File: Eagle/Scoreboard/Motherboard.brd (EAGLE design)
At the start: 67.3 x 92.7 mm, 27 parts

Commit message: Added capacitors for filtering
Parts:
- added C3, C4: 100n, capacitor-wima:C5B2.5
- C2: value 10u -> 47u
- moved REG 5.24 mm to (39.4, 73.7)
- moved C1 2.54 mm to (15.2, 77.5)
- moved C2 2.54 mm to (15.2, 68.6)
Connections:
- net 12V: now also C3.1
- net GND: now also C3.2, C4.2
- net VIN_9V: now also C4.1
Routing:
- net VIN_9V: track 40.2 -> 47.4 mm
- net 12V: track 36.9 -> 41.9 mm
- net GND: track 239.6 -> 244.4 mm
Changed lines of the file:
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@@
 <attribute name="OC_NEWARK" value="70K9898" x="60.96" y="40.64" size="1.778" layer="27" rot="R90" display="off"/>
 </element>
-<element name="C1" library="rcl" library_urn="urn:adsk.eagle:library:334" package="E2-4" package3d_urn="urn:adsk.eagle:package:23347/1" value="10u" x="17.78" y="77.47" rot="R270">
-<attribute name="SPICEPREFIX" value="C" x="17.78" y="77.47" size="1.778" layer="27" rot="R270" display="off"/>
-</element>
-<element name="C2" library="rcl" library_urn="urn:adsk.eagle:library:334" package="E2-4" package3d_urn="urn:adsk.eagle:package:23347/1" value="10u" x="17.78" y="68.58" rot="R90">
-<attribute name="SPICEPREFIX" value="C" x="17.78" y="68.58" size="1.778" layer="27" rot="R90" display="off"/>
+<element name="C1" library="rcl" library_urn="urn:adsk.eagle:library:334" package="E2-4" package3d_urn="urn:adsk.eagle:package:23347/1" value="10u" x="15.24" y="77.47" rot="R270">
+<attribute name="SPICEPREFIX" value="C" x="15.24" y="77.47" size="1.778" layer="27" rot="R270" display="off"/>
+</element>
+<element name="C2" library="rcl" library_urn="urn:adsk.eagle:library:334" package="E2-4" package3d_urn="urn:adsk.eagle:package:23347/1" value="47u" x="15.24" y="68.58" rot="R90">
+<attribute name="SPICEPREFIX" value="C" x="15.24" y="68.58" size="1.778" layer="27" rot="R90" display="off"/>
 </element>
 <element name="R1" library="resistor" library_urn="urn:adsk.eagle:library:348" package="0204/7" package3d_urn="urn:adsk.eagle:package:25945/1" value="10k" x="53.34" y="30.48" rot="R90"/>
@@
 <element name="R4" library="resistor" library_urn="urn:adsk.eagle:library:348" package="0204/7" package3d_urn="urn:adsk.eagle:package:25945/1" value="10k" x="45.72" y="30.48" rot="R90"/>
 <element name="R5" library="resistor" library_urn="urn:adsk.eagle:library:348" package="0204/7" package3d_urn="urn:adsk.eagle:package:25945/1" value="10k" x="40.64" y="30.48" rot="R90"/>
-<element name="REG" library="linear" library_urn="urn:adsk.eagle:library:262" package="TO220H" package3d_urn="urn:adsk.eagle:package:16414/1" value="LM7809" x="34.29" y="74.93" rot="R270"/>
+<element name="REG" library="linear" library_urn="urn:adsk.eagle:library:262" package="TO220H" package3d_urn="urn:adsk.eagle:package:16414/1" value="LM7809" x="39.37" y="73.66" rot="R270"/>
 <element name="SCORE" library="con-wago-500" library_urn="urn:adsk.eagle:library:195" package="W237-103" package3d_urn="urn:adsk.eagle:package:10691/1" value="" x="5.08" y="12.7" rot="R270">
 <attribute name="MF" value="" x="5.08" y="12.7" size="1.778" layer="27" rot="R270" display="off"/>
@@
 <attribute name="OC_NEWARK" value="70K9898" x="60.96" y="81.28" size="1.778" layer="27" rot="R90" display="off"/>
 </element>
+<element name="C3" library="capacitor-wima" library_urn="urn:adsk.eagle:library:116" package="C5B2.5" package3d_urn="urn:adsk.eagle:package:5426/1" value="100n" x="24.13" y="76.2" rot="R270"/>
+<element name="C4" library="capacitor-wima" library_urn="urn:adsk.eagle:library:116" package="C5B2.5" package3d_urn="urn:adsk.eagle:package:5426/1" value="100n" x="24.13" y="67.31" rot="R90"/>
 </elements>
 <signals>
@@
 <contactref element="R6" pad="2"/>
 <contactref element="LED" pad="2"/>
-<wire x1="17.78" y1="69.596" x2="13.97" y2="69.596" width="0.254" layer="16"/>
-<wire x1="13.97" y1="69.596" x2="4.786" y2="69.596" width="0.254" layer="16"/>
-<wire x1="4.786" y1="69.596" x2="3.81" y2="68.62" width="0.254" layer="16"/>
 <wire x1="19.09" y1="87.63" x2="19.09" y2="90.21" width="0.254" layer="16"/>
 <wire x1="19.09" y1="90.21" x2="20.32" y2="91.44" width="0.254" layer="16"/>
 <wire x1="20.32" y1="91.44" x2="29.21" y2="91.44" width="0.254" layer="16"/>
 <wire x1="29.21" y1="91.44" x2="33.02" y2="87.63" width="0.254" layer="16"/>
-<wire x1="17.78" y1="76.454" x2="17.78" y2="69.596" width="0.254" layer="16"/>
-<wire x1="17.78" y1="76.454" x2="19.304" y2="74.93" width="0.254" layer="16"/>
-<wire x1="19.304" y1="74.93" x2="24.13" y2="74.93" width="0.254" layer="16"/>
-<wire x1="24.13" y1="74.93" x2="30.48" y2="74.93" width="0.254" layer="16"/>
-<wire x1="30.48" y1="74.93" x2="33.02" y2="77.47" width="0.254" layer="16"/>
-<wire x1="33.02" y1="77.47" x2="33.02" y2="87.63" width="0.254" layer="16"/>
+<wire x1="33.02" y1="73.66" x2="35.56" y2="76.2" width="0.254" layer="16"/>
+<wire x1="35.56" y1="76.2" x2="35.56" y2="87.63" width="0.254" layer="16"/>
 <wire x1="20.32" y1="38.1" x2="24.13" y2="38.1" width="0.254" layer="16"/>
-<wire x1="13.97" y1="53.34" x2="16.51" y2="50.8" width="0.254" layer="16"/>
-<wire x1="16.51" y1="50.8" x2="22.86" y2="50.8" width="0.254" layer="16"/>
+<wire x1="22.86" y1="50.8" x2="16.51" y2="50.8" width="0.254" layer="16"/>
 <wire x1="22.86" y1="50.8" x2="24.13" y2="49.53" width="0.254" layer="16"/>
 <wire x1="24.13" y1="49.53" x2="24.13" y2="43.18" width="0.254" layer="16"/>
 <wire x1="24.13" y1="43.18" x2="24.13" y2="38.1" width="0.254" layer="16"/>
-<wire x1="13.97" y1="69.596" x2="13.97" y2="53.34" width="0.254" layer="16"/>
 <contactref element="433MHZ_VC" pad="1"/>
 <contactref element="INFRA_VC" pad="2"/>
@@
 <wire x1="65.837" y1="86.36" x2="65.837" y2="82.347" width="0.254" layer="16"/>
 <wire x1="65.837" y1="82.347" x2="62.23" y2="78.74" width="0.254" layer="16"/>
-<wire x1="47.03" y1="87.63" x2="33.02" y2="87.63" width="0.254" layer="16"/>
+<wire x1="47.03" y1="87.63" x2="35.56" y2="87.63" width="0.254" layer="16"/>
 <wire x1="40.64" y1="34.29" x2="43.18" y2="34.29" width="0.254" layer="16"/>
 <wire x1="43.18" y1="34.29" x2="45.72" y2="34.29" width="0.254" layer="16"/>
@@
 <vertex x="-2.54" y="93.98"/>
 </polygon>
+<contactref element="C3" pad="2"/>
+<contactref element="C4" pad="2"/>
+<wire x1="16.51" y1="50.8" x2="16.51" y2="53.34" width="0.3048" layer="16"/>
+<wire x1="16.51" y1="53.34" x2="10.16" y2="59.69" width="0.3048" layer="16"/>
+<wire x1="10.16" y1="59.69" x2="10.16" y2="69.596" width="0.3048" layer="16"/>
+<wire x1="35.56" y1="87.63" x2="33.02" y2="87.63" width="0.254" layer="16"/>
+<wire x1="29.21" y1="73.66" x2="24.13" y2="73.66" width="1.016" layer="16"/>
+<wire x1="24.13" y1="73.66" x2="24.13" y2="69.85" width="1.016" layer="16"/>
+<wire x1="15.24" y1="76.454" x2="15.24" y2="69.596" width="1.016" layer="16"/>
+<wire x1="15.24" y1="69.596" x2="4.786" y2="69.596" width="1.016" layer="16"/>
+<wire x1="4.786" y1="69.596" x2="3.81" y2="68.62" width="1.016" layer="16"/>
+<wire x1="15.24" y1="69.596" x2="23.876" y2="69.596" width="1.016" layer="16"/>
+<wire x1="23.876" y1="69.596" x2="24.13" y2="69.85" width="1.016" layer="16"/>
 </signal>
 <signal name="N$1">
@@
 <contactref element="R7" pad="2"/>
 <wire x1="8.93" y1="87.63" x2="13.93" y2="87.63" width="1.016" layer="16"/>
-<wire x1="24.09" y1="87.63" x2="24.13" y2="87.59" width="1.016" layer="16"/>
-<wire x1="24.13" y1="87.59" x2="24.13" y2="78.74" width="1.016" layer="16"/>
-<wire x1="24.13" y1="78.74" x2="24.13" y2="77.47" width="1.016" layer="16"/>
-<wire x1="11.557" y1="78.613" x2="13.97" y2="78.613" width="1.016" layer="16"/>
-<wire x1="13.97" y1="78.613" x2="17.653" y2="78.613" width="1.016" layer="16"/>
-<wire x1="17.653" y1="78.613" x2="17.78" y2="78.486" width="1.016" layer="16"/>
-<wire x1="17.78" y1="78.486" x2="23.876" y2="78.486" width="1.016" layer="16"/>
-<wire x1="23.876" y1="78.486" x2="24.13" y2="78.74" width="1.016" layer="16"/>
+<wire x1="13.97" y1="78.613" x2="15.24" y2="78.613" width="1.016" layer="16"/>
+<wire x1="15.24" y1="78.613" x2="15.24" y2="78.486" width="1.016" layer="16"/>
 <wire x1="13.93" y1="87.63" x2="13.93" y2="78.653" width="1.016" layer="16"/>
 <wire x1="13.93" y1="78.653" x2="13.97" y2="78.613" width="1.016" layer="16"/>
+<contactref element="C3" pad="1"/>
+<wire x1="11.557" y1="78.613" x2="13.97" y2="78.613" width="1.016" layer="16"/>
+<wire x1="15.24" y1="78.486" x2="15.494" y2="78.74" width="1.016" layer="16"/>
+<wire x1="15.494" y1="78.74" x2="24.13" y2="78.74" width="1.016" layer="16"/>
+<wire x1="24.13" y1="78.74" x2="26.67" y2="78.74" width="1.016" layer="16"/>
+<wire x1="26.67" y1="78.74" x2="29.21" y2="76.2" width="1.016" layer="16"/>
+<wire x1="24.13" y1="78.74" x2="24.13" y2="87.59" width="1.016" layer="16"/>
+<wire x1="24.13" y1="87.59" x2="24.09" y2="87.63" width="1.016" layer="16"/>
 </signal>
 <signal name="TXD">
@@
 <contactref element="C2" pad="+"/>
 <contactref element="ARDUINO_NANO1" pad="15"/>
-<wire x1="17.78" y1="67.564" x2="24.13" y2="67.564" width="1.016" layer="16"/>
-<wire x1="24.13" y1="67.31" x2="24.13" y2="72.39" width="1.016" layer="16"/>
-<wire x1="24.13" y1="67.564" x2="24.13" y2="67.31" width="1.016" layer="16"/>
+<wire x1="29.21" y1="71.12" x2="27.94" y2="71.12" width="1.016" layer="16"/>
 <wire x1="24.13" y1="53.34" x2="31.75" y2="45.72" width="1.016" layer="16"/>
 <wire x1="31.75" y1="45.72" x2="35.56" y2="45.72" width="1.016" layer="16"/>
-<wire x1="24.13" y1="67.31" x2="24.13" y2="53.34" width="1.016" layer="16"/>
+<contactref element="C4" pad="1"/>
+<wire x1="29.21" y1="71.12" x2="29.21" y2="67.31" width="1.016" layer="16"/>
+<wire x1="29.21" y1="67.31" x2="26.67" y2="64.77" width="1.016" layer="16"/>
+<wire x1="26.67" y1="64.77" x2="24.13" y2="64.77" width="1.016" layer="16"/>
+<wire x1="24.13" y1="64.77" x2="24.13" y2="53.34" width="1.016" layer="16"/>
+<wire x1="24.13" y1="64.77" x2="17.78" y2="64.77" width="1.016" layer="16"/>
+<wire x1="17.78" y1="64.77" x2="15.24" y2="67.31" width="1.016" layer="16"/>
+<wire x1="15.24" y1="67.31" x2="15.24" y2="67.564" width="1.016" layer="16"/>
 </signal>
 <signal name="VCC">

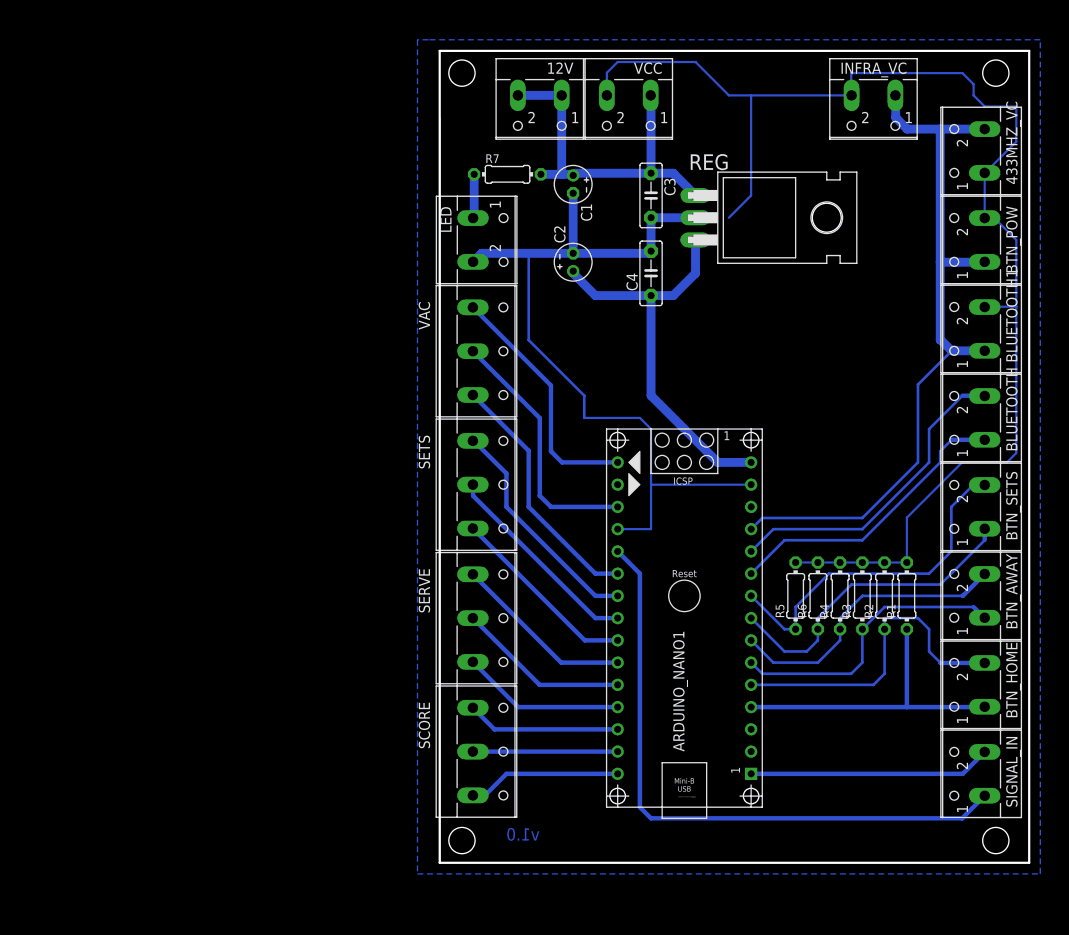
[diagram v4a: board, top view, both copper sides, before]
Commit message: Added polygon and make more space for screws
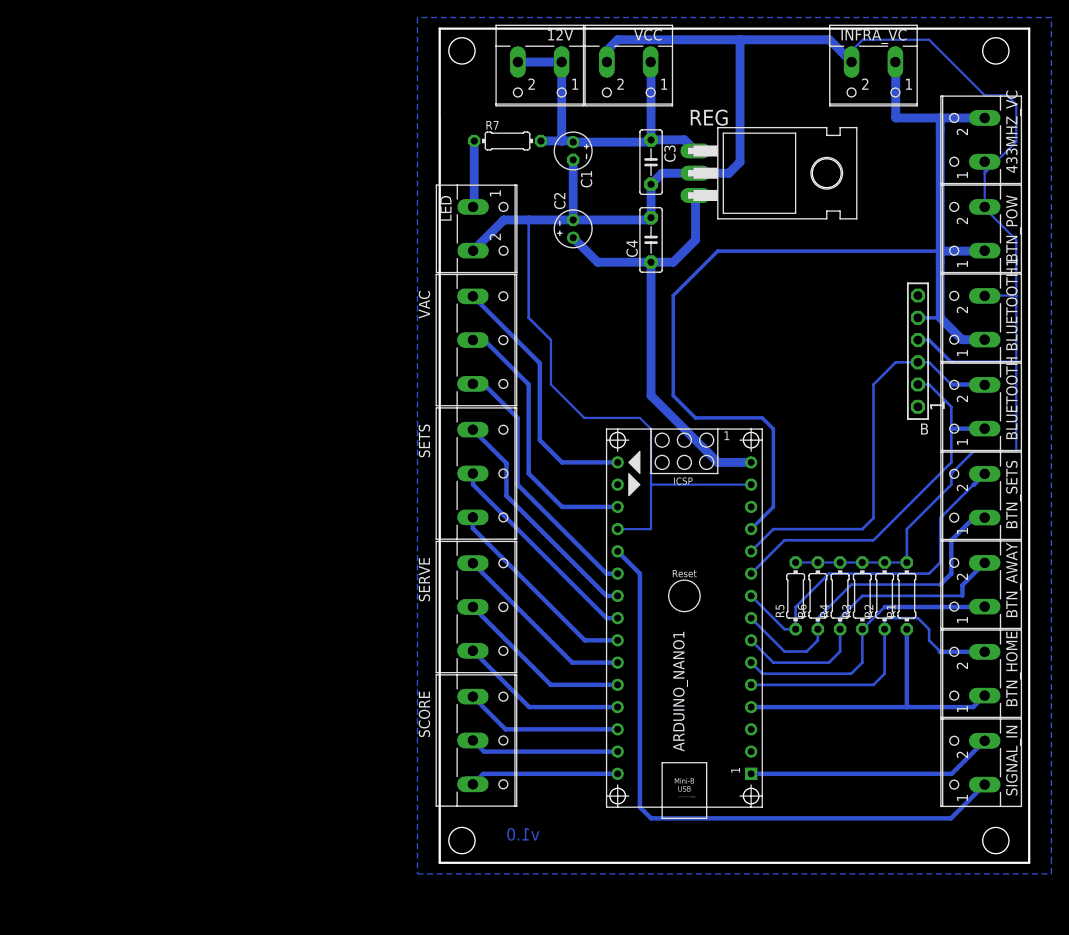
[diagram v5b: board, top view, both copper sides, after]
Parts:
- added B: SSW-106-02-G-S, con-samtec:SSW-106-02-G-S
- moved REG 5.08 mm to (39.4, 78.7)
- moved 12V 3.81 mm to (11.4, 90.2)
- moved C1 3.81 mm to (15.2, 81.3)
- moved C2 3.81 mm to (15.2, 72.4)
- moved C3 3.81 mm to (24.1, 80.0)
- moved C4 3.81 mm to (24.1, 71.1)
- moved INFRA_VC 3.81 mm to (49.5, 90.2)
- moved R7 3.81 mm to (7.75, 82.4)
- moved VCC 3.81 mm to (21.6, 90.2)
- moved BLUETOOTH 1.27 mm to (61.0, 52.1)
- moved SETS 1.27 mm to (5.08, 44.5)
- moved SCORE 1.27 mm to (5.08, 14.0)
- moved BTN_AWAY 1.27 mm to (61.0, 31.8)
- moved BTN_HOME 1.27 mm to (61.0, 21.6)
- moved SERVE 1.27 mm to (5.08, 29.2)
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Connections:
- net GND: now also B.4
- net RXD: now also ARDUINO_NANO1.10, B.2, BLUETOOTH.1; no longer ARDUINO_NANO1.11, BLUETOOTH.2
- net TXD: now also ARDUINO_NANO1.11, B.3, BLUETOOTH.2; no longer ARDUINO_NANO1.10, BLUETOOTH.1
- net VCC: now also B.5
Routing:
- net VCC: track 84.6 -> 122.6 mm
- net GND: track 244.4 -> 265.5 mm
- net TXD: track 33.7 -> 45.6 mm
- net RXD: track 36.3 -> 43.2 mm
- net VIN_9V: track 47.4 -> 51.1 mm
- net N$7: track 5.05 -> 7.59 mm
- net N$4: track 33.4 -> 35.4 mm
- net N$5: track 36.3 -> 38.3 mm
- net RESET: track 29.1 -> 30.4 mm
- net SETS_3: track 21.8 -> 23.1 mm
- net VAC1: track 28.3 -> 29.5 mm
- net VAC3: track 28.7 -> 30.0 mm
- net N$2: track 37.2 -> 36.0 mm
- net 12V: track 41.9 -> 41.3 mm
- net SERVE_2: track 19.7 -> 20.2 mm
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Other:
- board size 67.3 x 92.7 mm -> 67.3 x 95.2 mm

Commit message: Fixed error with A6, A7 pin plus couple major changes
The pin A6 & A7 cannot be used for anything digital on Nano. So removed
Also moved the bluetooth pins and removed buttons for sets to get some free pin.  Made the bluetooth module powered by 3.3V so we don't need to use voltage divider. Also made the 9V available so we can use it for powering all the score controllers
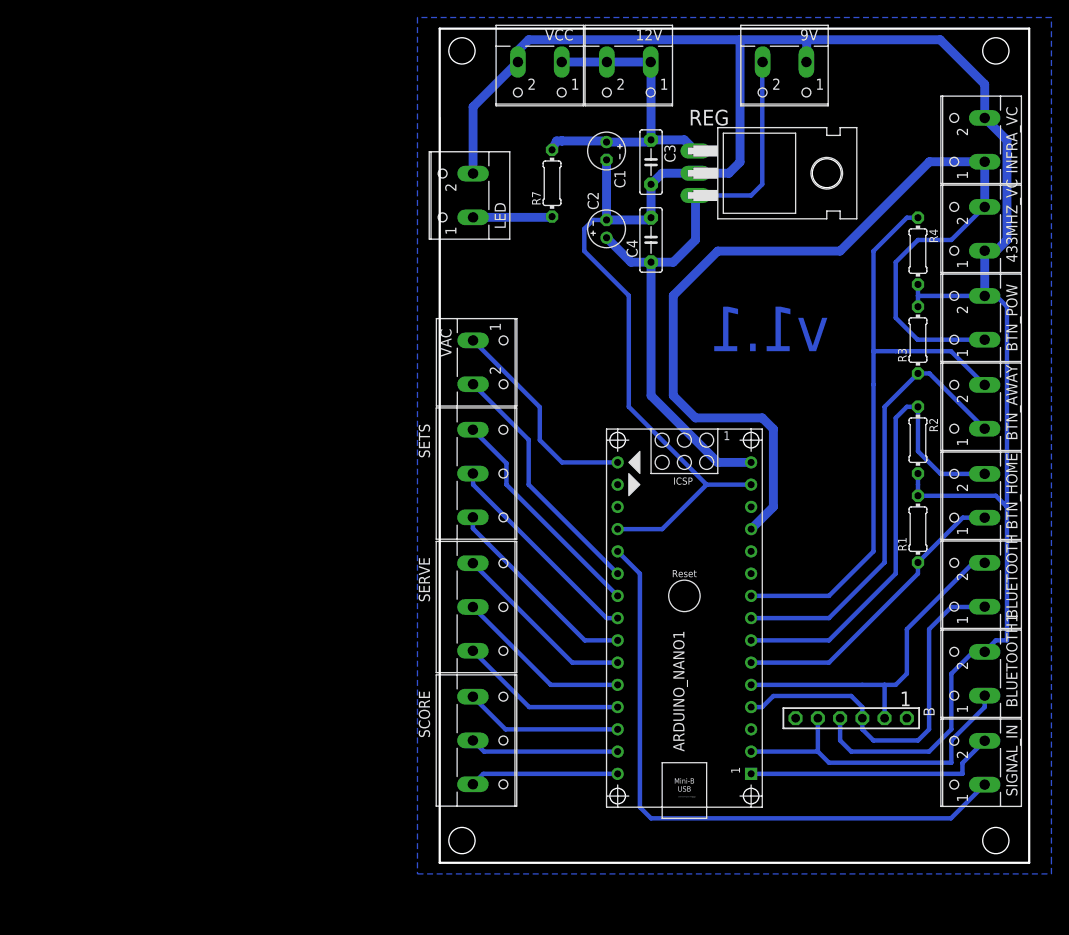
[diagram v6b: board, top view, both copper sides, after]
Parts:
- removed BTN_SETS: (no value), con-wago-500:W237-102
- removed R5, R6: 10k, resistor:0204/7
- added 9V: (no value), con-wago-500:W237-102
- VAC: device con-wago-500:W237-103 -> con-wago-500:W237-102
- moved B 42.6 mm to (47.0, 16.5), turned to 180 degrees
- moved BLUETOOTH1 40.6 mm to (61.0, 21.6)
- moved R4 40.4 mm to (54.6, 69.8), turned to 270 degrees
- moved R3 29.9 mm to (54.6, 59.7)
- moved BLUETOOTH 20.3 mm to (61.0, 31.8)
- moved BTN_AWAY 20.3 mm to (61.0, 52.1)
- moved BTN_HOME 20.3 mm to (61.0, 41.9)
- moved R2 18.2 mm to (54.6, 48.3), turned to 270 degrees
- moved INFRA_VC 13.7 mm to (61.0, 82.5), turned to 90 degrees
- moved BTN_POW 10.2 mm to (61.0, 62.2)
- moved 12V 10.2 mm to (21.6, 90.2)
- moved VCC 10.2 mm to (11.4, 90.2)
- moved 433MHZ_VC 10.2 mm to (61.0, 72.4)
- moved R1 7.73 mm to (54.6, 38.1)
- moved R7 7.01 mm to (12.8, 77.6), turned to 90 degrees
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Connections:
- net VAC1 renamed N$6
- removed net N$6 (its old number): ARDUINO_NANO1.9, BTN_SETS.2, R5.1
- removed net RESET: ARDUINO_NANO1.18, VAC.2
- removed net VAC3: ARDUINO_NANO1.21, VAC.3
- new net 3V3: ARDUINO_NANO1.2, B.5, BLUETOOTH1.1
- net GND: now also 9V.1; no longer R5.2, R6.2
- net N$1: now also ARDUINO_NANO1.6; no longer ARDUINO_NANO1.4
- net N$2: now also ARDUINO_NANO1.7; no longer ARDUINO_NANO1.5
- net N$3: now also ARDUINO_NANO1.8; no longer ARDUINO_NANO1.6
- net N$4: now also ARDUINO_NANO1.9; no longer ARDUINO_NANO1.7
- net N$5: now also ARDUINO_NANO1.21, VAC.2; no longer ARDUINO_NANO1.8, BTN_SETS.1, R6.1
- net RXD: now also ARDUINO_NANO1.5, BLUETOOTH.2; no longer ARDUINO_NANO1.10, BLUETOOTH.1
- net TXD: now also ARDUINO_NANO1.4, BLUETOOTH.1; no longer ARDUINO_NANO1.11, BLUETOOTH.2
- net VCC: no longer B.5, BLUETOOTH1.1
- net VIN_9V: now also 9V.2
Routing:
- net N$6 (its old number): track 40.1 -> 0.00 mm
- net 3V3: track 0.00 -> 36.4 mm
- net N$4: track 35.4 -> 71.3 mm
- net RESET: track 30.4 -> 0.00 mm
- net VAC3: track 30.0 -> 0.00 mm
- net GND: track 265.5 -> 293.9 mm
- net N$3: track 32.6 -> 51.3 mm
- net VIN_9V: track 51.1 -> 69.4 mm
- net N$2: track 36.0 -> 54.3 mm
- net N$5: track 38.3 -> 28.5 mm
- net VCC: track 122.6 -> 114.3 mm
- net N$6: track 29.5 -> 24.5 mm
- net 12V: track 41.3 -> 36.8 mm
- net RXD: track 43.2 -> 39.2 mm
- net N$1: track 36.1 -> 34.3 mm
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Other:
- board text added: "v1.1"
- board text removed: "v1.0"

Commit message: Fixed connection plan, added pins
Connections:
- net N$1 renamed A2
- net N$2 renamed A3
- net N$3 renamed A4
- net N$4 renamed A5
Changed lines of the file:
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@@
 <wire x1="43.18" y1="16.51" x2="43.18" y2="12.7" width="0.508" layer="16"/>
 </signal>
-<signal name="N$1">
+<signal name="A2">
 <contactref element="BTN_HOME" pad="1"/>
 <contactref element="ARDUINO_NANO1" pad="6"/>
@@
 <wire x1="54.61" y1="33.02" x2="54.61" y2="34.29" width="0.508" layer="16"/>
 </signal>
-<signal name="N$2">
+<signal name="A3">
 <contactref element="ARDUINO_NANO1" pad="7"/>
 <contactref element="BTN_HOME" pad="2"/>
@@
 <wire x1="57.19" y1="44.41" x2="62.23" y2="44.41" width="0.508" layer="16"/>
 </signal>
-<signal name="N$3">
+<signal name="A4">
 <contactref element="ARDUINO_NANO1" pad="8"/>
 <contactref element="BTN_AWAY" pad="1"/>
@@
 <wire x1="55.92" y1="55.88" x2="54.61" y2="55.88" width="0.508" layer="16"/>
 </signal>
-<signal name="N$4">
+<signal name="A5">
 <contactref element="ARDUINO_NANO1" pad="9"/>
 <contactref element="BTN_AWAY" pad="2"/>
